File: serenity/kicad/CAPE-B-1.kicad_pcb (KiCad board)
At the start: 4 copper layers, 55 x 35 mm, 39 parts

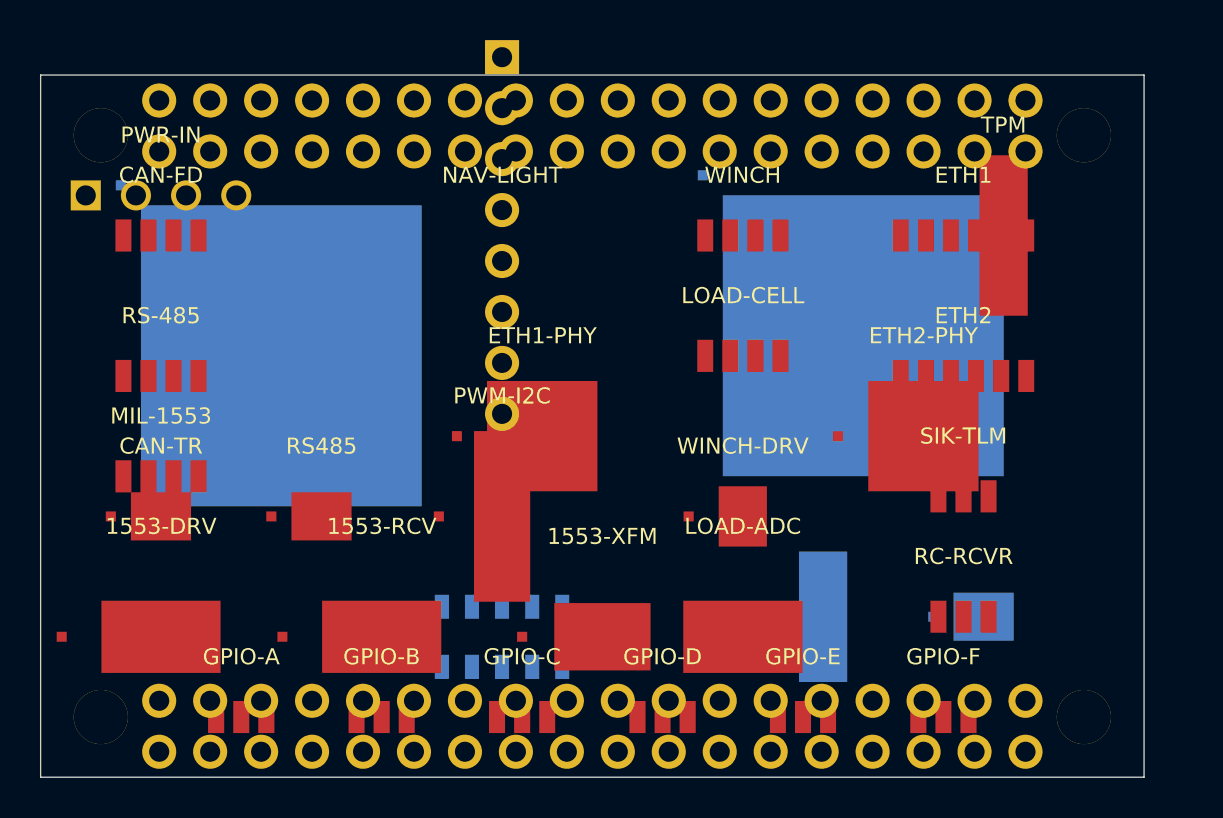
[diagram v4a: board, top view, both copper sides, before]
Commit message: Consolidate wired data link connectors to left edge on both capes
Move all five external wired data link connectors to the left edge
(X=127) in matching positions on both CAPE-A-1 and CAPE-B-1:

  Y=94  CAN-FD  (4-pin JST-GH)
  Y=99  RS-485  (4-pin JST-GH)
  Y=104 MIL-1553 (4-pin JST-GH)
  Y=109 ETH1     (6-pin JST-GH)  ← moved from right side
  Y=114 ETH2     (6-pin JST-GH)  ← moved from right side

Right side (X=167) retains only non-wired-link connectors:
  CAPE-A: ESC-TLM, PWR-IN
  CAPE-B: SIK-TLM, RC-RCVR, PWR-IN (relocated from left to free the top
          of the data-link column)

https://claude.ai/code/session_01GniMw4QukTVM7JMzyVjH6p
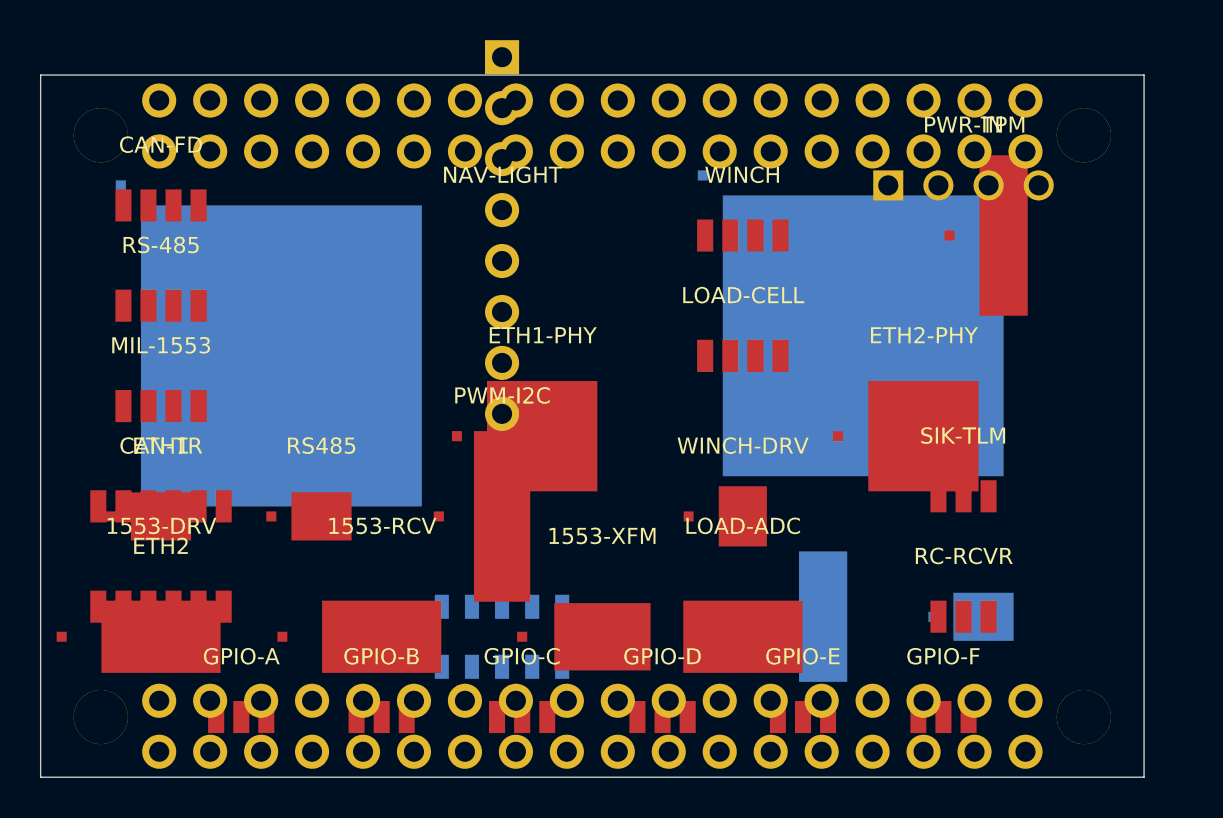
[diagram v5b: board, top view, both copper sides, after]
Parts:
- moved ETH1 42.2 mm to (127.0, 109.0)
- moved ETH2 41.6 mm to (127.0, 114.0)
- moved PWR-IN 40.0 mm to (167.0, 93.0)
- moved MIL-1553 3.50 mm to (127.0, 104.0)
- moved RS-485 3.50 mm to (127.0, 99.0)
- moved CAN-FD 1.50 mm to (127.0, 94.0)
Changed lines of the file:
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@@
     (pad "9" smd rect (at 1.5 1.5) (size 0.7 1.2) (layers "B.Cu" "B.Paste" "B.Mask"))
     (pad "10" smd rect (at 3.0 1.5) (size 0.7 1.2) (layers "B.Cu" "B.Paste" "B.Mask")))
-  (footprint "JST_GH_4P" (layer "F.Cu") (at 127 95.5) (property "Description" "CAN FD external connector — GND CAN_H CAN_L +3V3")
+  (footprint "JST_GH_4P" (layer "F.Cu") (at 127 94) (property "Description" "CAN FD external connector — GND CAN_H CAN_L +3V3")
     (fp_text reference "CAN-FD" (at 0 -3) (layer "F.SilkS")
       (effects (font (size 0.8 0.8) (thickness 0.15))))
@@
     (pad "3" smd rect (at 0.625 0) (size 0.8 1.6) (layers "F.Cu" "F.Paste" "F.Mask"))
     (pad "4" smd rect (at 1.875 0) (size 0.8 1.6) (layers "F.Cu" "F.Paste" "F.Mask")))
-  (footprint "JST_GH_4P" (layer "F.Cu") (at 127 102.5) (property "Description" "RS-485 external connector — GND RS485_A RS485_B +3V3")
+  (footprint "JST_GH_4P" (layer "F.Cu") (at 127 99) (property "Description" "RS-485 external connector — GND RS485_A RS485_B +3V3")
     (fp_text reference "RS-485" (at 0 -3) (layer "F.SilkS")
       (effects (font (size 0.8 0.8) (thickness 0.15))))
@@
     (pad "3" smd rect (at 0.625 0) (size 0.8 1.6) (layers "F.Cu" "F.Paste" "F.Mask"))
     (pad "4" smd rect (at 1.875 0) (size 0.8 1.6) (layers "F.Cu" "F.Paste" "F.Mask")))
-  (footprint "JST_GH_4P" (layer "F.Cu") (at 127 107.5) (property "Description" "MIL-STD-1553 bus connector — GND BUS_1553_A_P BUS_1553_A_N GND")
+  (footprint "JST_GH_4P" (layer "F.Cu") (at 127 104) (property "Description" "MIL-STD-1553 bus connector — GND BUS_1553_A_P BUS_1553_A_N GND")
     (fp_text reference "MIL-1553" (at 0 -3) (layer "F.SilkS")
       (effects (font (size 0.8 0.8) (thickness 0.15))))
@@
     (pad "3" smd rect (at 0.625 0) (size 0.8 1.6) (layers "F.Cu" "F.Paste" "F.Mask"))
     (pad "4" smd rect (at 1.875 0) (size 0.8 1.6) (layers "F.Cu" "F.Paste" "F.Mask")))
-  (footprint "JST_GH_6P" (layer "F.Cu") (at 167 95.5) (property "Description" "Ethernet 1 MagJack — ETH1_TX_P ETH1_TX_N GND GND ETH1_RX_P ETH1_RX_N")
+  (footprint "JST_GH_6P" (layer "F.Cu") (at 127 109) (property "Description" "Ethernet 1 MagJack — ETH1_TX_P ETH1_TX_N GND GND ETH1_RX_P ETH1_RX_N")
     (fp_text reference "ETH1" (at 0 -3) (layer "F.SilkS")
       (effects (font (size 0.8 0.8) (thickness 0.15))))
@@
     (pad "5" smd rect (at 1.875 0) (size 0.8 1.6) (layers "F.Cu" "F.Paste" "F.Mask"))
     (pad "6" smd rect (at 3.125 0) (size 0.8 1.6) (layers "F.Cu" "F.Paste" "F.Mask")))
-  (footprint "JST_GH_6P" (layer "F.Cu") (at 167 102.5) (property "Description" "Ethernet 2 MagJack — ETH2_TX_P ETH2_TX_N GND GND ETH2_RX_P ETH2_RX_N")
+  (footprint "JST_GH_6P" (layer "F.Cu") (at 127 114) (property "Description" "Ethernet 2 MagJack — ETH2_TX_P ETH2_TX_N GND GND ETH2_RX_P ETH2_RX_N")
     (fp_text reference "ETH2" (at 0 -3) (layer "F.SilkS")
       (effects (font (size 0.8 0.8) (thickness 0.15))))
@@
     (pad "2" smd rect (at 0.0 0) (size 0.8 1.6) (layers "F.Cu" "F.Paste" "F.Mask"))
     (pad "3" smd rect (at 1.25 0) (size 0.8 1.6) (layers "F.Cu" "F.Paste" "F.Mask")))
-  (footprint "Connector_Molex_NanoFit" (layer "F.Cu") (at 127 93.5) (property "Description" "Molex Nano-Fit 4-pin 5V power input — +5V +5V GND GND")
+  (footprint "Connector_Molex_NanoFit" (layer "F.Cu") (at 167 93) (property "Description" "Molex Nano-Fit 4-pin 5V power input — +5V +5V GND GND")
     (fp_text reference "PWR-IN" (at 0 -3) (layer "F.SilkS")
       (effects (font (size 0.8 0.8) (thickness 0.15))))

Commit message: Fix critical placement errors and reduce courtyard overlaps on both capes
P0 fixes (board boundary violations — pad holes were outside Edge.Cuts):
- CAPE-A: Move SERVO header (141,103) from (150,94.5); pad 1 now at Y=94.11,
  inside board top (87.5), clears PB2-P1 lower socket row by 2mm
- CAPE-B: Move NAV-LIGHT header to (174,104) from (144,95.5); all 8 pads
  inside board, no conflict with mounting hole at (173,90.5) or PB2-P1 socket

P1 fixes (courtyard overlaps):
- CAPE-A: Move IMU to (130,96.5) and BARO to (136,96.5), each up 2mm;
  eliminates both chips' CrtYd overlap with ETH1-PHY at Y=99.25
- CAPE-A: Move ETH2-PHY to (161,103.5) from (165,103.5); 1.05mm gap to
  TPM CrtYd, up from −2.95mm (was overlapping)
- CAPE-B: NAV-LIGHT at X=174 gives 0.8mm clearance to TPM CrtYd

Remaining P1 courtyard overlaps (require KiCad interactive editor):
- CAPE-A: SERVO/GPS CrtYd edge-to-edge 0.6mm gap (within DRC tolerance);
  1553-XFM vs TPM (2.7mm × 2.9mm overlap in dense right-side cluster)
- CAPE-B: ETH1-PHY vs PWM-I2C; PWM-I2C vs 1553-RCV and 1553-XFM
  (inherent to the high-density comms cape layout)

Note: both boards remain placement-only (no routed traces, copper pour,
or vias). Full fabrication readiness requires KiCad router, DRC, and
Gerber/drill file export.

https://claude.ai/code/session_01GniMw4QukTVM7JMzyVjH6p
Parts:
- moved NAV-LIGHT 31.2 mm to (174.0, 104.0)
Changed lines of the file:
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@@
     (pad "3" smd rect (at 0.625 0) (size 0.8 1.6) (layers "F.Cu" "F.Paste" "F.Mask"))
     (pad "4" smd rect (at 1.875 0) (size 0.8 1.6) (layers "F.Cu" "F.Paste" "F.Mask")))
-  (footprint "Connector_PinHeader_2.54mm" (layer "F.Cu") (at 144 95.5) (property "Description" "1x8 nav light PWM header 2.54mm TH — PCA9685 PWM_CH0-3 GND GND +3V3 +5V")
+  (footprint "Connector_PinHeader_2.54mm" (layer "F.Cu") (at 174 104) (property "Description" "1x8 nav light PWM header 2.54mm TH — PCA9685 PWM_CH0-3 GND GND +3V3 +5V")
     (fp_text reference "NAV-LIGHT" (at 0 -3) (layer "F.SilkS")
       (effects (font (size 0.8 0.8) (thickness 0.15))))
